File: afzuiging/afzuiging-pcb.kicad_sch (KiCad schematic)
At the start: 15 parts, among them J1 Voeding 15V, J2 Signaal 0-10V, J3 Signaal 0-10V, U2 ESP32_DevKit_V1_DOIT, U3 L7805, U4 MCP6002-xP

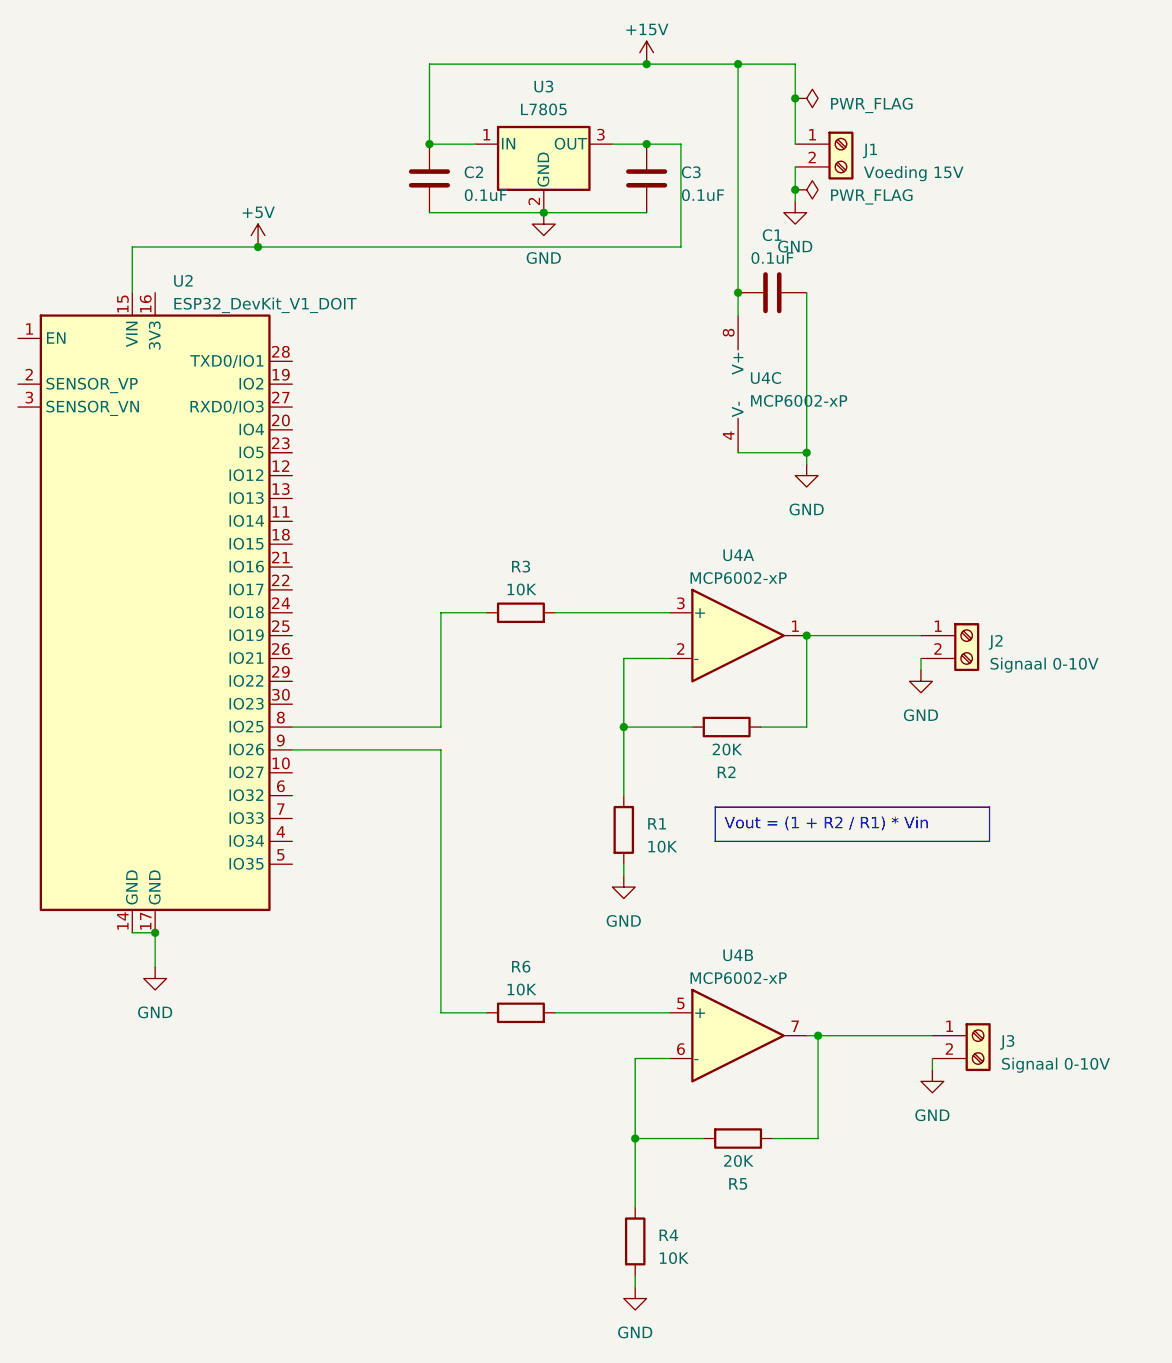
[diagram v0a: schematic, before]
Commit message: Use OpAmp NE5532N
NE5532N can actually be used for 10 volt. MCP6002 has a maximum voltage of 6 volt.
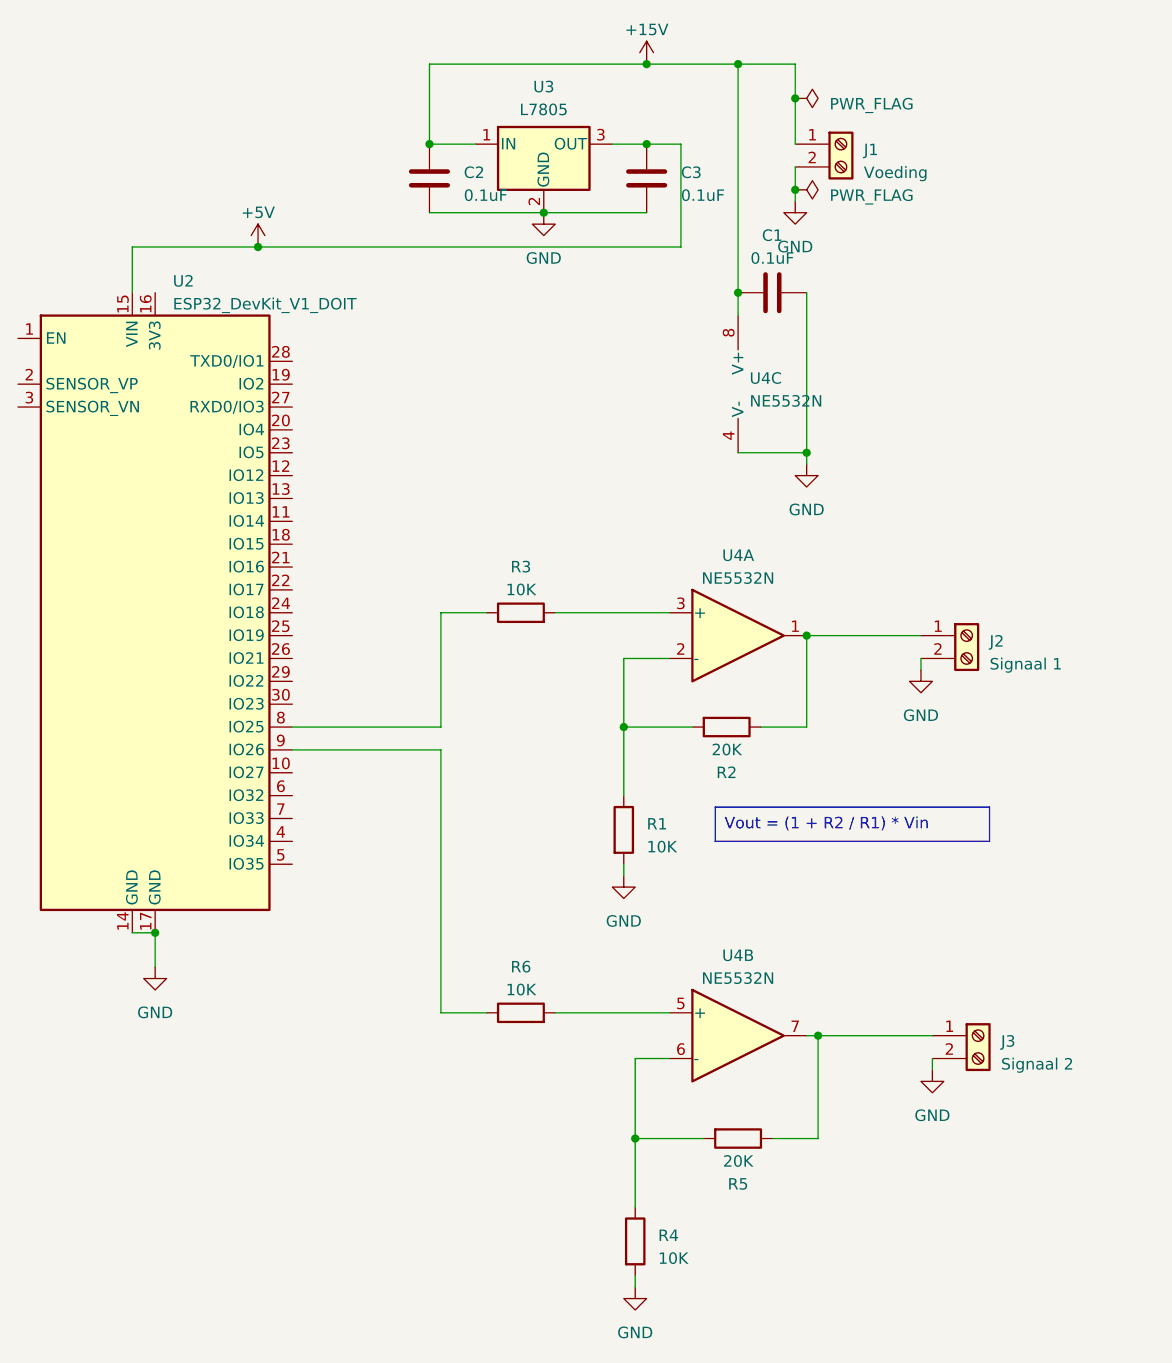
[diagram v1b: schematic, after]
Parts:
- J1: value Voeding 15V -> Voeding
- J2: value Signaal 0-10V -> Signaal 1
- J3: value Signaal 0-10V -> Signaal 2
- U4: value MCP6002-xP -> NE5532N
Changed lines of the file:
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@@
       (effects (font (size 1.27 1.27)))
     )
-    (property "Value" "MCP6002-xP" (at 119.38 121.92 0)
+    (property "Value" "NE5532N" (at 119.38 121.92 0)
       (effects (font (size 1.27 1.27)))
     )
@@
       (effects (font (size 1.27 1.27)) hide)
     )
-    (property "Datasheet" "http://ww1.microchip.com/downloads/en/DeviceDoc/21733j.pdf" (at 119.38 128.27 0)
+    (property "Datasheet" "https://www.ti.com/lit/ds/symlink/ne5532.pdf" (at 119.38 128.27 0)
       (effects (font (size 1.27 1.27)) hide)
     )
@@
       (effects (font (size 1.27 1.27)) (justify left))
     )
-    (property "Value" "Signaal 0-10V" (at 147.32 86.995 0)
+    (property "Value" "Signaal 1" (at 147.32 86.995 0)
       (effects (font (size 1.27 1.27)) (justify left))
     )
@@
       (effects (font (size 1.27 1.27)) (justify left))
     )
-    (property "Value" "MCP6002-xP" (at 120.65 57.785 0)
+    (property "Value" "NE5532N" (at 120.65 57.785 0)
       (effects (font (size 1.27 1.27)) (justify left))
     )
@@
       (effects (font (size 1.27 1.27)) hide)
     )
-    (property "Datasheet" "http://ww1.microchip.com/downloads/en/DeviceDoc/21733j.pdf" (at 121.92 55.88 0)
+    (property "Datasheet" "https://www.ti.com/lit/ds/symlink/ne5532.pdf" (at 121.92 55.88 0)
       (effects (font (size 1.27 1.27)) hide)
     )
@@
       (effects (font (size 1.27 1.27)))
     )
-    (property "Value" "MCP6002-xP" (at 119.38 77.47 0)
+    (property "Value" "NE5532N" (at 119.38 77.47 0)
       (effects (font (size 1.27 1.27)))
     )
@@
       (effects (font (size 1.27 1.27)) hide)
     )
-    (property "Datasheet" "http://ww1.microchip.com/downloads/en/DeviceDoc/21733j.pdf" (at 119.38 83.82 0)
+    (property "Datasheet" "https://www.ti.com/lit/ds/symlink/ne5532.pdf" (at 119.38 83.82 0)
       (effects (font (size 1.27 1.27)) hide)
     )
@@
       (effects (font (size 1.27 1.27)) (justify left))
     )
-    (property "Value" "Signaal 0-10V" (at 148.59 131.445 0)
+    (property "Value" "Signaal 2" (at 148.59 131.445 0)
       (effects (font (size 1.27 1.27)) (justify left))
     )
@@
       (effects (font (size 1.27 1.27)) (justify left))
     )
-    (property "Value" "Voeding 15V" (at 133.35 32.385 0)
-      (effects (font (size 1.27 1.27)) (justify left))
-    )
+    (property "Value" "Voeding" (at 133.35 32.385 0)
+      (effects (font (size 1.27 1.27)) (justify left))
+    )
